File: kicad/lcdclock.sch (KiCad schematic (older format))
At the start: 25 parts, among them CON1 AVR-ISP, SW1 RESET, U1 ATTINY24A, U2 AY0438, U3 AY0438, U4 LCD_DE377, U5 CONRAD_DCF, Y1 32.768kHz/12.5pF

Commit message: Route PCB
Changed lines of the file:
@@
 L TEST TP2
 U 1 1 59BAA1CF
+P 5200 2600
+F 0 "TP2" H 5200 2900 50  0000 C BNN
+F 1 "DDAT" H 5200 2850 50  0000 C CNN
+F 2 "Measurement_Points:Measurement_Point_Round-SMD-Pad_Big" H 5200 2600 50  0001 C CNN
+F 3 "" H 5200 2600 50  0001 C CNN
+	1    5200 2600
+	1    0    0    -1
+$EndComp
+$Comp
+L TEST TP3
+U 1 1 59BAA21E
 P 5000 2600
-F 0 "TP2" H 5000 2900 50  0000 C BNN
-F 1 "DDAT" H 5000 2850 50  0000 C CNN
+F 0 "TP3" H 5000 2900 50  0000 C BNN
+F 1 "DCLK" H 5000 2850 50  0000 C CNN
 F 2 "Measurement_Points:Measurement_Point_Round-SMD-Pad_Big" H 5000 2600 50  0001 C CNN
 F 3 "" H 5000 2600 50  0001 C CNN
 	1    5000 2600
-	1    0    0    -1
-$EndComp
-$Comp
-L TEST TP3
-U 1 1 59BAA21E
-P 5200 2600
-F 0 "TP3" H 5200 2900 50  0000 C BNN
-F 1 "DCLK" H 5200 2850 50  0000 C CNN
-F 2 "Measurement_Points:Measurement_Point_Round-SMD-Pad_Big" H 5200 2600 50  0001 C CNN
-F 3 "" H 5200 2600 50  0001 C CNN
-	1    5200 2600
 	1    0    0    -1
 $EndComp
@@
 	4800 2700 4800 2600
 Connection ~ 4800 2700
-Wire Wire Line
-	5000 2600 5000 2800
-Connection ~ 5000 2800
-Wire Wire Line
-	5200 2600 5200 2900
-Connection ~ 5200 2900
 Connection ~ 4300 6150
 Wire Wire Line
@@
 	6350 8150 8550 8150
 Wire Wire Line
-	6150 8350 8550 8350
-Wire Wire Line
-	6250 3250 8550 3250
-Wire Wire Line
-	6250 2800 6250 3250
+	6250 2800 6250 8350
 Connection ~ 6350 3150
 Wire Wire Line
 	8550 3150 6350 3150
-Wire Wire Line
-	8550 3350 6150 3350
-Connection ~ 6150 3350
-Wire Wire Line
-	6150 2900 6150 8350
 Wire Wire Line
 	6350 2700 6350 8150
@@
 NoConn ~ 9850 9600
 NoConn ~ 9850 9500
+Wire Wire Line
+	5000 2600 5000 2800
+Connection ~ 5000 2800
+Wire Wire Line
+	5200 2600 5200 2900
+Connection ~ 5200 2900
+Wire Wire Line
+	6250 3350 8550 3350
+Connection ~ 6250 3350
+Wire Wire Line
+	6250 8350 8550 8350
+Wire Wire Line
+	6150 2900 6150 3250
+Wire Wire Line
+	6150 3250 8550 3250
 $EndSCHEMATC

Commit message: Rework for a STM32 CPU
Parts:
- removed CON1: AVR-ISP, Connectors:IDC_Header_Straight_6pins, symbol AVR-ISP-6
- removed R1: 10k, Resistors_SMD:R_0805_HandSoldering, symbol R
- removed R2, R3: 0, Resistors_SMD:R_0805_HandSoldering, symbol R
- removed TP1: DLOA, Measurement_Points:Measurement_Point_Round-SMD-Pad_Big, symbol TEST
- removed TP2: DDAT, Measurement_Points:Measurement_Point_Round-SMD-Pad_Big, symbol TEST
- removed TP3: DCLK, Measurement_Points:Measurement_Point_Round-SMD-Pad_Big, symbol TEST
- removed TP6: CLK, Measurement_Points:Measurement_Point_Round-SMD-Pad_Big, symbol TEST
- removed U1: ATTINY24A, Housings_SOIC:SOIC-14_3.9x8.7mm_Pitch1.27mm, symbol ATTINY24A-SSU
- removed U2, U3: AY0438, Housings_DIP:DIP-40_W15.24mm, symbol AY0438
- removed U5: CONRAD_DCF, LCD Clock:CONNECTOR_4x1, symbol ELV_DCF-2
- added C10, C6, C7, C8: 100n, Resistors_SMD:R_0805_HandSoldering, symbol C
- added C11, C12: 15p, Resistors_SMD:R_0805_HandSoldering, symbol C
- added C9: 1u, Resistors_SMD:R_0805_HandSoldering, symbol C
- added J1: Conn_JLink_SWD, symbol Conn_JLink_SWD
- added U1: STM32L073V8, Housings_QFP:LQFP-100_14x14mm_Pitch0.5mm, symbol STM32L073xx_LQFP100
- added U2: ELV_DCF-2, symbol ELV_DCF-2
- C1: value 100n -> 10u
- C4: value 120p -> 100n
- SW1: value RESET -> SW_Push; footprint Buttons_Switches_SMD:SW_SPST_PTS645 -> (none)
- Y1: value 32.768kHz/12.5pF -> 32.768kHz 12.5pF; footprint LCD Clock:MS1V-T1K -> (none)
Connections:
- wire segments 150 -> 87
- no-connect marks 17 -> 10
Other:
- note removed: "Placeholders for Caps.\nDo not connect if absent."
- moved on the sheet: C5, L1

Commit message: Change LCD and CPU to 48 pins
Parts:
- removed BT1: 3.6V Lithium AA, LCD Clock:CONNECTOR_2x1, symbol 3.6V_Lithium_AA
- removed C2: 100n, Resistors_SMD:R_0805_HandSoldering, symbol C
- removed D1: BAT60A, Diodes_SMD:D_SOD-323_HandSoldering, symbol D
- removed U1: STM32L073V8, Housings_QFP:LQFP-100_14x14mm_Pitch0.5mm, symbol STM32L073xx_LQFP100
- removed U4: LCD_DE377, LCD Clock:LCD-DIP, symbol LCD_DE377
- added BT1: 4xAA 6.4-3.2V, symbol Battery
- added C13: 2.2u, symbol C
- added C14: 1u, symbol C
- added D1: LED, symbol LED
- added R1: 100k, symbol R
- added U1: STM32L073xx_48, symbol STM32L073xx_48
- added U3: TPS70630, symbol TPS706xx
- added U4: LCD, symbol LCD
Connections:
- net labels added: VCC
- net labels removed: +BATT
- wire segments 87 -> 105
- no-connect marks 10 -> 13
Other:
- note added: "Backlight\nDo not connect if not needed."
- moved on the sheet: C1, C10, C11, C12, C3, C4, C5, C6, C7, C8, C9, J1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

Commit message: Select parts and assign footprints
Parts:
- removed TP4: TVCC, Measurement_Points:Measurement_Point_Round-SMD-Pad_Big, symbol TEST
- removed TP5: TSIG, Measurement_Points:Measurement_Point_Round-SMD-Pad_Big, symbol TEST
- BT1, D1: footprint (none) -> LCD Clock:CONNECTOR_2x1
- C13, C14, R1: footprint (none) -> Resistors_SMD:R_0805_HandSoldering
- J1: footprint (none) -> Connectors:IDC_Header_Straight_20pins
- L1: footprint LCD Clock:WE_470uH_Inductor -> Resistors_SMD:R_1812_HandSoldering
- SW1: footprint (none) -> Buttons_Switches_SMD:SW_SPST_B3S-1000
- U1: footprint (none) -> Housings_QFP:LQFP-48_7x7mm_Pitch0.5mm
- U2: footprint (none) -> LCD Clock:CONNECTOR_3x1
- U3: footprint (none) -> TO_SOT_Packages_SMD:SOT-23-5_HandSoldering
- U4: footprint (none) -> Connectors:IDC_Header_Straight_16pins
- Y1: footprint (none) -> Crystals:Crystal_SMD_SeikoEpson_MC405-2pin_9.6x4.1mm_HandSoldering
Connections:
- wire segments 105 -> 103
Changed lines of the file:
@@
 F 0 "L1" H 1200 5700 50  0000 C CNN
 F 1 "470u" V 1360 5700 50  0000 C CNN
-F 2 "LCD Clock:WE_470uH_Inductor" H 1250 5700 50  0001 C CNN
+F 2 "Resistors_SMD:R_1812_HandSoldering" H 1250 5700 50  0001 C CNN
 F 3 "" H 1250 5700 50  0001 C CNN
 	1    1250 5700
@@
 	0    -1   -1   0
 $EndComp
-$Comp
-L TEST TP4
-U 1 1 59BAD22D
-P 1550 5850
-F 0 "TP4" H 1550 6150 50  0000 C BNN
-F 1 "TVCC" H 1550 6100 50  0000 C CNN
-F 2 "Measurement_Points:Measurement_Point_Round-SMD-Pad_Big" H 1550 5850 50  0001 C CNN
-F 3 "" H 1550 5850 50  0001 C CNN
-	1    1550 5850
-	1    0    0    -1
-$EndComp
-$Comp
-L TEST TP5
-U 1 1 59BAD5C4
-P 1750 6450
-F 0 "TP5" H 1750 6750 50  0000 C BNN
-F 1 "TSIG" H 1750 6700 50  0000 C CNN
-F 2 "Measurement_Points:Measurement_Point_Round-SMD-Pad_Big" H 1750 6450 50  0001 C CNN
-F 3 "" H 1750 6450 50  0001 C CNN
-	1    1750 6450
-	1    0    0    -1
-$EndComp
 Wire Wire Line
 	1650 6550 1850 6550
@@
 F 0 "SW1" H 4600 5750 50  0000 L CNN
 F 1 "SW_Push" H 4550 5590 50  0000 C CNN
-F 2 "" H 4550 5850 50  0001 C CNN
+F 2 "Buttons_Switches_SMD:SW_SPST_B3S-1000" H 4550 5850 50  0001 C CNN
 F 3 "" H 4550 5850 50  0001 C CNN
 	1    4550 5650
@@
 F 0 "J1" H 5400 6800 50  0000 L CNN
 F 1 "Conn_JLink_SWD" H 6100 5600 50  0000 R CNN
-F 2 "" H 5750 6250 50  0001 C CNN
+F 2 "Connectors:IDC_Header_Straight_20pins" H 5750 6250 50  0001 C CNN
 F 3 "" H 5750 6250 50  0001 C CNN
 	1    5750 6250
@@
 	5100 5850 5200 5850
 Wire Wire Line
-	1750 6550 1750 6450
-Connection ~ 1750 6550
-Wire Wire Line
 	2750 6550 2850 6550
 Wire Wire Line
@@
 $EndComp
 Wire Wire Line
-	1550 5950 1550 5850
-Wire Wire Line
 	1850 5950 1850 5750
-Connection ~ 1550 5950
 Wire Wire Line
 	750  7150 1250 7150
@@
 F 0 "Y1" H 2050 4100 50  0000 C CNN
 F 1 "32.768kHz 12.5pF" H 2050 3800 50  0000 C CNN
-F 2 "" H 2050 3950 50  0001 C CNN
+F 2 "Crystals:Crystal_SMD_SeikoEpson_MC405-2pin_9.6x4.1mm_HandSoldering" H 2050 3950 50  0001 C CNN
 F 3 "" H 2050 3950 50  0001 C CNN
 	1    2050 3950
@@
 F 0 "U2" H 1050 6900 60  0000 L CNN
 F 1 "ELV_DCF-2" H 1250 6200 60  0000 L CNN
-F 2 "" H 1250 6550 60  0001 C CNN
+F 2 "LCD Clock:CONNECTOR_3x1" H 1250 6550 60  0001 C CNN
 F 3 "" H 1250 6550 60  0001 C CNN
 	1    1250 6550
@@
 F 0 "U3" H 1900 2000 60  0000 L CNN
 F 1 "TPS70630" H 2150 1400 60  0000 L CNN
-F 2 "" H 2150 1700 60  0001 C CNN
+F 2 "TO_SOT_Packages_SMD:SOT-23-5_HandSoldering" H 2150 1700 60  0001 C CNN
 F 3 "" H 2150 1700 60  0001 C CNN
 	1    2150 1700
@@
 F 0 "C14" H 2975 2050 50  0000 L CNN
 F 1 "1u" H 2975 1850 50  0000 L CNN
-F 2 "" H 2988 1800 50  0001 C CNN
+F 2 "Resistors_SMD:R_0805_HandSoldering" H 2988 1800 50  0001 C CNN
 F 3 "" H 2950 1950 50  0001 C CNN
 	1    2950 1950
@@
 F 0 "C13" H 2725 2050 50  0000 L CNN
 F 1 "2.2u" H 2725 1850 50  0000 L CNN
-F 2 "" H 2738 1800 50  0001 C CNN
+F 2 "Resistors_SMD:R_0805_HandSoldering" H 2738 1800 50  0001 C CNN
 F 3 "" H 2700 1950 50  0001 C CNN
 	1    2700 1950
@@
 F 0 "U4" H 9700 2950 60  0000 L CNN
 F 1 "LCD" H 10750 1050 60  0000 R CNN
-F 2 "" H 9900 3800 60  0001 C CNN
+F 2 "Connectors:IDC_Header_Straight_16pins" H 9900 3800 60  0001 C CNN
 F 3 "" H 9900 3800 60  0001 C CNN
 	1    10150 2050
@@
 F 0 "BT1" H 950 1800 50  0000 L CNN
 F 1 "4xAA 6.4-3.2V" H 950 1700 50  0000 L CNN
-F 2 "" V 850 1760 50  0001 C CNN
+F 2 "LCD Clock:CONNECTOR_2x1" V 850 1760 50  0001 C CNN
 F 3 "" V 850 1760 50  0001 C CNN
 	1    850  1700
@@
 F 0 "U1" V 5400 2550 60  0000 R CNN
 F 1 "STM32L073xx_48" V 6250 1850 60  0000 L CNN
-F 2 "" H 6200 1950 60  0001 C CNN
+F 2 "Housings_QFP:LQFP-48_7x7mm_Pitch0.5mm" H 6200 1950 60  0001 C CNN
 F 3 "" H 6200 1950 60  0001 C CNN
 	1    5950 2200
@@
 F 0 "U1" H 7850 3650 60  0000 L CNN
 F 1 "STM32L073xx_48" H 8400 950 60  0000 R CNN
-F 2 "" H 8600 2150 60  0001 C CNN
+F 2 "Housings_QFP:LQFP-48_7x7mm_Pitch0.5mm" H 8600 2150 60  0001 C CNN
 F 3 "" H 8600 2150 60  0001 C CNN
 	2    8350 2400
@@
 F 0 "U1" H 3900 6400 60  0000 L CNN
 F 1 "STM32L073xx_48" H 4250 5800 60  0000 R CNN
-F 2 "" H 4500 5850 60  0001 C CNN
+F 2 "Housings_QFP:LQFP-48_7x7mm_Pitch0.5mm" H 4500 5850 60  0001 C CNN
 F 3 "" H 4500 5850 60  0001 C CNN
 	3    4250 6100
@@
 F 0 "U1" H 2050 6700 60  0000 L CNN
 F 1 "STM32L073xx_48" H 2550 6400 60  0000 R CNN
-F 2 "" H 2550 6300 60  0001 C CNN
+F 2 "Housings_QFP:LQFP-48_7x7mm_Pitch0.5mm" H 2550 6300 60  0001 C CNN
 F 3 "" H 2550 6300 60  0001 C CNN
 	4    2300 6550
@@
 F 0 "U1" H 1200 4350 60  0000 L CNN
 F 1 "STM32L073xx_48" H 1700 3550 60  0000 R CNN
-F 2 "" H 1750 3700 60  0001 C CNN
+F 2 "Housings_QFP:LQFP-48_7x7mm_Pitch0.5mm" H 1750 3700 60  0001 C CNN
 F 3 "" H 1750 3700 60  0001 C CNN
 	5    1500 3950
@@
 F 0 "D1" H 10250 3450 50  0000 C CNN
 F 1 "LED" H 10250 3250 50  0000 C CNN
-F 2 "" H 10250 3350 50  0001 C CNN
+F 2 "LCD Clock:CONNECTOR_2x1" H 10250 3350 50  0001 C CNN
 F 3 "" H 10250 3350 50  0001 C CNN
 	1    10250 3350
@@
 F 0 "R1" V 9930 3350 50  0000 C CNN
 F 1 "100k" V 9850 3350 50  0000 C CNN
-F 2 "" V 9780 3350 50  0001 C CNN
+F 2 "Resistors_SMD:R_0805_HandSoldering" V 9780 3350 50  0001 C CNN
 F 3 "" H 9850 3350 50  0001 C CNN
 	1    9850 3350

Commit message: Layout PCB
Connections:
- wire segments 103 -> 107
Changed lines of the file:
@@
 Connection ~ 5950 1550
-Wire Wire Line
-	8600 1300 9500 1300
-Wire Wire Line
-	8600 1400 9500 1400
-Wire Wire Line
-	8600 1500 9500 1500
-Wire Wire Line
-	8600 1600 9500 1600
 Wire Wire Line
 	8600 1800 9500 1800
@@
 	0    1    1    0
 $EndComp
+Wire Wire Line
+	8600 1600 9500 1600
+Wire Wire Line
+	8600 1400 9500 1400
+Wire Wire Line
+	8600 1300 9100 1300
+Wire Wire Line
+	9400 1500 9500 1500
+Wire Wire Line
+	9100 1300 9400 1500
+Wire Wire Line
+	8600 1500 9050 1500
+Wire Wire Line
+	9050 1500 9250 1300
+Wire Wire Line
+	9250 1300 9500 1300
 $EndSCHEMATC

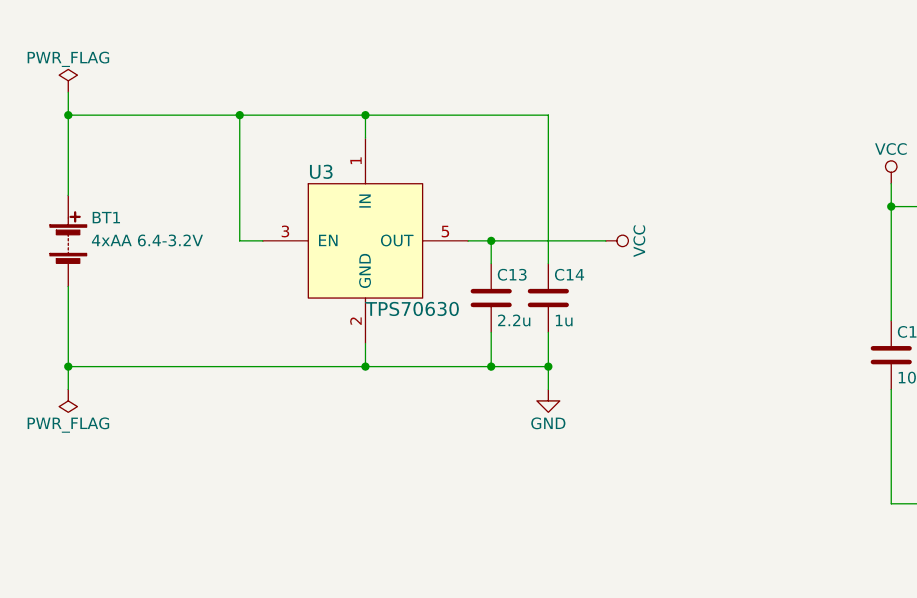
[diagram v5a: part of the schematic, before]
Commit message: Add reverse voltage protection
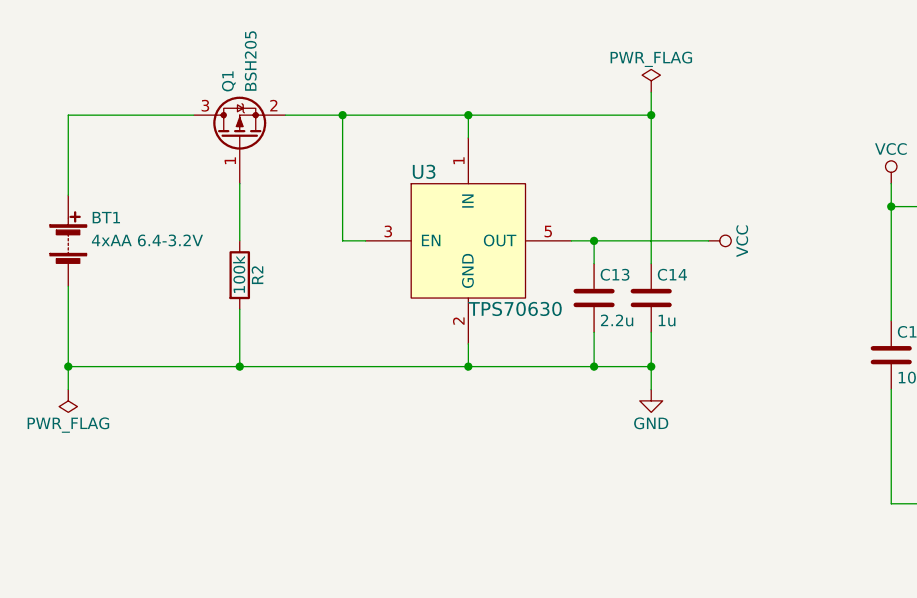
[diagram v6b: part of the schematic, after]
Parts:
- added Q1: BSH205, TO_SOT_Packages_SMD:SOT-23_Handsoldering, symbol Q_PMOS_GSD
- added R2: 100k, Resistors_SMD:R_0805_HandSoldering, symbol R
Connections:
- wire segments 107 -> 110
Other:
- moved on the sheet: C13, C14, U3
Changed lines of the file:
@@
 L GND #PWR01
 U 1 1 59B7CB4A
-P 2950 2350
-F 0 "#PWR01" H 2950 2100 50  0001 C CNN
-F 1 "GND" H 2950 2200 50  0000 C CNN
-F 2 "" H 2950 2350 50  0001 C CNN
-F 3 "" H 2950 2350 50  0001 C CNN
-	1    2950 2350
+P 3400 2350
+F 0 "#PWR01" H 3400 2100 50  0001 C CNN
+F 1 "GND" H 3400 2200 50  0000 C CNN
+F 2 "" H 3400 2350 50  0001 C CNN
+F 3 "" H 3400 2350 50  0001 C CNN
+	1    3400 2350
 	1    0    0    -1
 $EndComp
@@
 L TPS706xx U3
 U 1 1 59C2A669
-P 2150 1700
-F 0 "U3" H 1900 2000 60  0000 L CNN
-F 1 "TPS70630" H 2150 1400 60  0000 L CNN
-F 2 "TO_SOT_Packages_SMD:SOT-23-5_HandSoldering" H 2150 1700 60  0001 C CNN
-F 3 "" H 2150 1700 60  0001 C CNN
-	1    2150 1700
+P 2600 1700
+F 0 "U3" H 2350 2000 60  0000 L CNN
+F 1 "TPS70630" H 2600 1400 60  0000 L CNN
+F 2 "TO_SOT_Packages_SMD:SOT-23-5_HandSoldering" H 2600 1700 60  0001 C CNN
+F 3 "" H 2600 1700 60  0001 C CNN
+	1    2600 1700
 	1    0    0    -1
 $EndComp
@@
 L C C14
 U 1 1 59C2C059
-P 2950 1950
-F 0 "C14" H 2975 2050 50  0000 L CNN
-F 1 "1u" H 2975 1850 50  0000 L CNN
-F 2 "Resistors_SMD:R_0805_HandSoldering" H 2988 1800 50  0001 C CNN
-F 3 "" H 2950 1950 50  0001 C CNN
-	1    2950 1950
-	1    0    0    -1
-$EndComp
-Wire Wire Line
-	2150 1150 2150 1250
-Wire Wire Line
-	2150 2250 2150 2150
-Wire Wire Line
-	2600 1700 3200 1700
-Wire Wire Line
-	2700 1700 2700 1800
-Wire Wire Line
-	2700 2250 2700 2100
-Connection ~ 2150 2250
+P 3400 1950
+F 0 "C14" H 3425 2050 50  0000 L CNN
+F 1 "1u" H 3425 1850 50  0000 L CNN
+F 2 "Resistors_SMD:R_0805_HandSoldering" H 3438 1800 50  0001 C CNN
+F 3 "" H 3400 1950 50  0001 C CNN
+	1    3400 1950
+	1    0    0    -1
+$EndComp
+Wire Wire Line
+	2600 1150 2600 1250
+Wire Wire Line
+	2600 2250 2600 2150
+Wire Wire Line
+	3050 1700 3650 1700
+Wire Wire Line
+	3150 1700 3150 1800
+Wire Wire Line
+	3150 2250 3150 2100
+Connection ~ 2600 2250
 $Comp
 L C C13
 U 1 1 59C2C8A9
-P 2700 1950
-F 0 "C13" H 2725 2050 50  0000 L CNN
-F 1 "2.2u" H 2725 1850 50  0000 L CNN
-F 2 "Resistors_SMD:R_0805_HandSoldering" H 2738 1800 50  0001 C CNN
-F 3 "" H 2700 1950 50  0001 C CNN
-	1    2700 1950
-	1    0    0    -1
-$EndComp
-Wire Wire Line
-	850  1050 850  1500
-Wire Wire Line
-	2950 1150 2950 1800
-Connection ~ 2150 1150
-Wire Wire Line
-	2950 2100 2950 2350
-Connection ~ 2700 2250
-Wire Wire Line
-	850  1150 2950 1150
-Wire Wire Line
-	850  2250 2950 2250
-Wire Wire Line
-	1700 1700 1600 1700
-Wire Wire Line
-	1600 1700 1600 1150
-Connection ~ 1600 1150
-Connection ~ 2700 1700
+P 3150 1950
+F 0 "C13" H 3175 2050 50  0000 L CNN
+F 1 "2.2u" H 3175 1850 50  0000 L CNN
+F 2 "Resistors_SMD:R_0805_HandSoldering" H 3188 1800 50  0001 C CNN
+F 3 "" H 3150 1950 50  0001 C CNN
+	1    3150 1950
+	1    0    0    -1
+$EndComp
+Wire Wire Line
+	3400 1050 3400 1800
+Connection ~ 2600 1150
+Wire Wire Line
+	3400 2100 3400 2350
+Connection ~ 3150 2250
+Wire Wire Line
+	1800 1150 3400 1150
+Wire Wire Line
+	850  2250 3400 2250
+Wire Wire Line
+	2150 1700 2050 1700
+Wire Wire Line
+	2050 1700 2050 1150
+Connection ~ 2050 1150
+Connection ~ 3150 1700
 $Comp
 L VCC #PWR09
 U 1 1 59C304BD
-P 3200 1700
-F 0 "#PWR09" H 3200 1550 50  0001 C CNN
-F 1 "VCC" H 3200 1850 50  0000 C CNN
-F 2 "" H 3200 1700 50  0001 C CNN
-F 3 "" H 3200 1700 50  0001 C CNN
-	1    3200 1700
+P 3650 1700
+F 0 "#PWR09" H 3650 1550 50  0001 C CNN
+F 1 "VCC" H 3650 1850 50  0000 C CNN
+F 2 "" H 3650 1700 50  0001 C CNN
+F 3 "" H 3650 1700 50  0001 C CNN
+	1    3650 1700
 	0    1    1    0
 $EndComp
@@
 	1    0    0    -1
 $EndComp
-Connection ~ 2950 2250
+Connection ~ 3400 2250
 $Comp
 L LCD U4
@@
 L PWR_FLAG #FLG014
 U 1 1 59C37520
-P 850 1050
-F 0 "#FLG014" H 850 1125 50  0001 C CNN
-F 1 "PWR_FLAG" H 850 1200 50  0000 C CNN
-F 2 "" H 850 1050 50  0001 C CNN
-F 3 "" H 850 1050 50  0001 C CNN
-	1    850  1050
-	1    0    0    -1
-$EndComp
-Connection ~ 850  1150
+P 3400 1050
+F 0 "#FLG014" H 3400 1125 50  0001 C CNN
+F 1 "PWR_FLAG" H 3400 1200 50  0000 C CNN
+F 2 "" H 3400 1050 50  0001 C CNN
+F 3 "" H 3400 1050 50  0001 C CNN
+	1    3400 1050
+	1    0    0    -1
+$EndComp
 Wire Wire Line
 	850  1900 850  2350
@@
 Wire Wire Line
 	9250 1300 9500 1300
+$Comp
+L Q_PMOS_GSD Q1
+U 1 1 59C3A539
+P 1600 1250
+F 0 "Q1" H 1800 1300 50  0000 L CNN
+F 1 "BSH205" H 1800 1200 50  0000 L CNN
+F 2 "TO_SOT_Packages_SMD:SOT-23_Handsoldering" H 1800 1350 50  0001 C CNN
+F 3 "" H 1600 1250 50  0001 C CNN
+	1    1600 1250
+	0    -1   -1   0
+$EndComp
+Wire Wire Line
+	1400 1150 850  1150
+Connection ~ 1600 2250
+Connection ~ 3400 1150
+Wire Wire Line
+	850  1150 850  1500
+$Comp
+L R R2
+U 1 1 59C3B737
+P 1600 1850
+F 0 "R2" V 1680 1850 50  0000 C CNN
+F 1 "100k" V 1600 1850 50  0000 C CNN
+F 2 "Resistors_SMD:R_0805_HandSoldering" V 1530 1850 50  0001 C CNN
+F 3 "" H 1600 1850 50  0001 C CNN
+	1    1600 1850
+	1    0    0    -1
+$EndComp
+Wire Wire Line
+	1600 1700 1600 1450
+Wire Wire Line
+	1600 2000 1600 2250
 $EndSCHEMATC

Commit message: Replace crystal Y1 footprint with a smaller one
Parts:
- Y1: footprint Crystals:Crystal_SMD_SeikoEpson_MC405-2pin_9.6x4.1mm_HandSoldering -> Crystals:Crystal_SMD_SeikoEpson_MC405-2pin_9.6x4.1mm
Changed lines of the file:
@@
 F 0 "Y1" H 2050 4100 50  0000 C CNN
 F 1 "32.768kHz 12.5pF" H 2050 3800 50  0000 C CNN
-F 2 "Crystals:Crystal_SMD_SeikoEpson_MC405-2pin_9.6x4.1mm_HandSoldering" H 2050 3950 50  0001 C CNN
+F 2 "Crystals:Crystal_SMD_SeikoEpson_MC405-2pin_9.6x4.1mm" H 2050 3950 50  0001 C CNN
 F 3 "" H 2050 3950 50  0001 C CNN
 	1    2050 3950

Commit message: Final fixes
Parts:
- BT1: value 4xAA 6.4-3.2V -> 4xAAA 6.4-3.2V
- R1: value 100k -> ?
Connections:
- wire segments 110 -> 111
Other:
- moved on the sheet: C1, C3, C4, C6, C7, C8, C9
